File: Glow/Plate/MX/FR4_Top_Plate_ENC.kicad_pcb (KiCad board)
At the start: 2 copper layers, 139.1 x 107.7 mm, 35 parts, among them SW1 SW_PUSH, SW10 SW_PUSH, SW11 SW_PUSH, SW12 SW_PUSH, SW13 SW_PUSH, SW14 SW_PUSH, SW15 SW_PUSH, SW16 SW_PUSH, SW17 SW_PUSH, SW18 SW_PUSH, SW19 SW_PUSH, SW2 SW_PUSH, SW20 SW_PUSH, SW21 SW_PUSH, SW22 SW_PUSH, SW23 SW_PUSH, SW24 SW_PUSH, SW25 SW_PUSH, SW26 SW_PUSH, SW27 SW_PUSH, SW28 SW_PUSH, SW29 SW_PUSH, SW3 SW_PUSH, SW30 Rotary_Encoder_Switch, SW4 SW_PUSH, SW5 SW_PUSH, SW6 SW_PUSH, SW7 SW_PUSH, SW8 SW_PUSH, SW9 SW_PUSH

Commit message: Blank front plate option added
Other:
- rule pad_to_mask_clearance: 0.2 -> 0

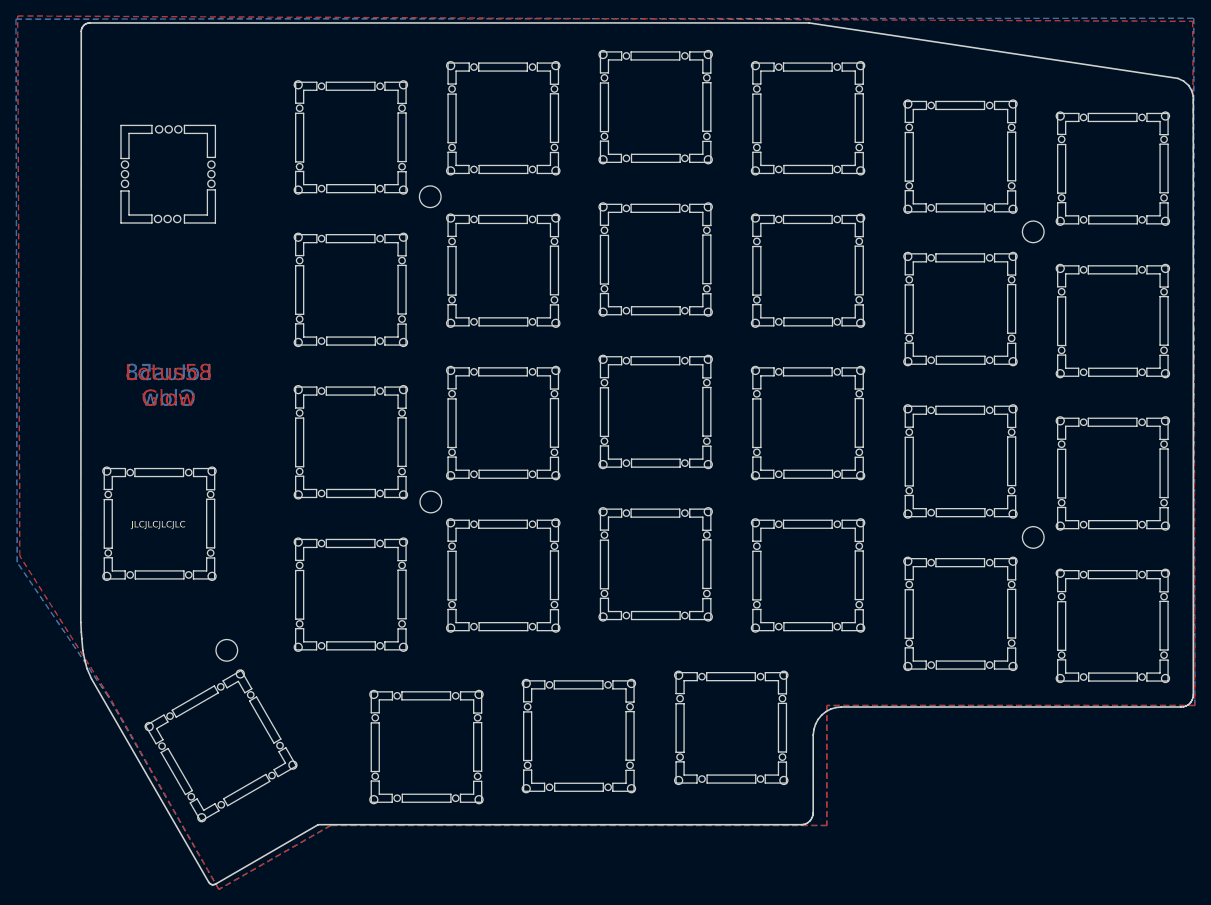
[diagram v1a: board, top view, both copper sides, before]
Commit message: Updated plates to remove break-away parts
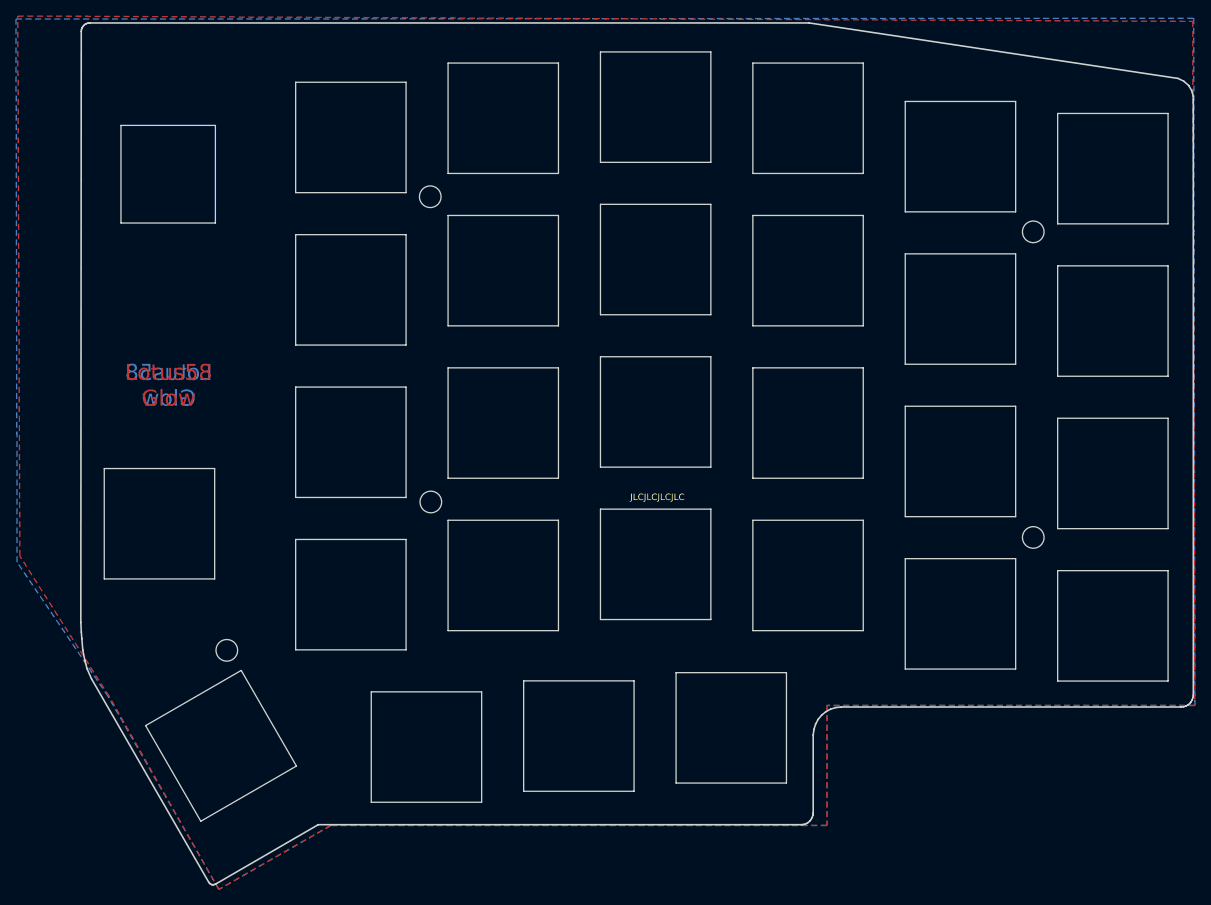
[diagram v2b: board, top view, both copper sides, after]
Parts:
- SW1, SW10, SW11, SW12, SW13, SW14, SW15, SW16, SW17, SW18, SW19, SW2, SW20, SW21, SW22, SW23, SW24, SW25, SW26, SW27, SW28, SW29, SW3, SW4, SW5, SW6, SW7, SW8, SW9: footprint Keyboard Library:Cherry_MX_Plate_Hole_Breakoff -> Keyboard Library:Cherry_MX_Plate_Hole_Placeholder
- SW30: footprint Keyboard Library:RotaryEncoder_PlateHole_Breakoff -> Keyboard Library:RotaryEncoder_PlateHole_Placeholder
